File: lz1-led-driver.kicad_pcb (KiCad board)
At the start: 2 copper layers, 80 x 20.5 mm, 41 parts, among them J1 BarrelJack_3167288, J2 USB4105-GF-A, U1 MP2483DQ-LF-P, U2 AP62301Z6-7, U3 SM02B-SRSS-TB-LF-SN, U4 SM02B-SRSS-TB-LF-SN

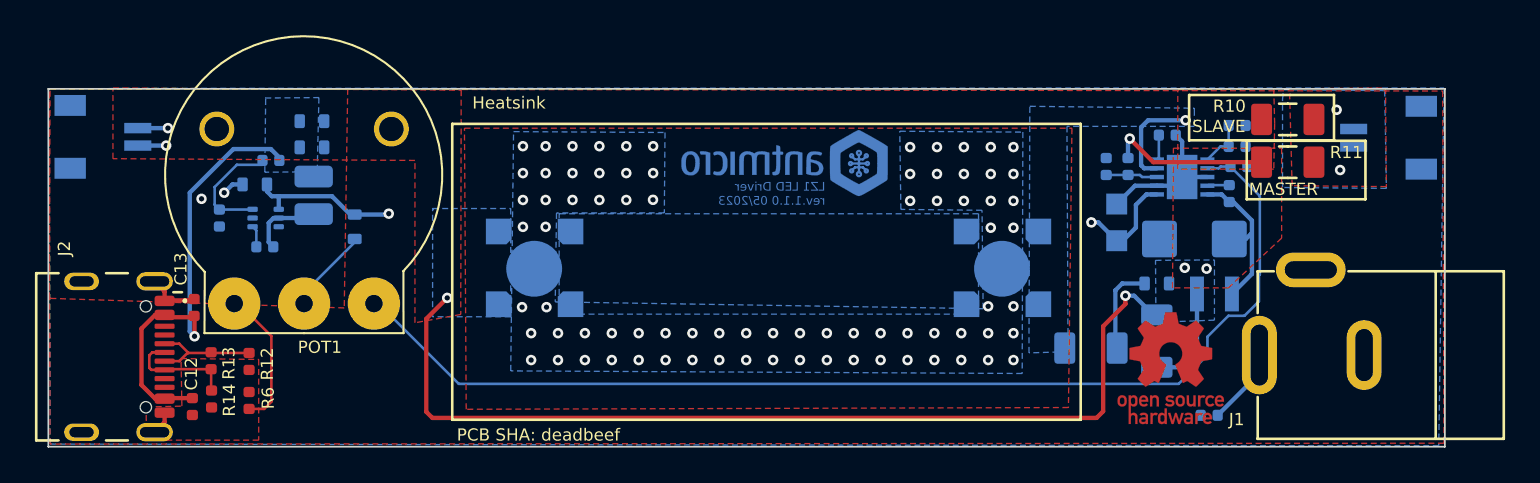
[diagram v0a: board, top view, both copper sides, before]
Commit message: Correct symbols and footprints with missing 3D models
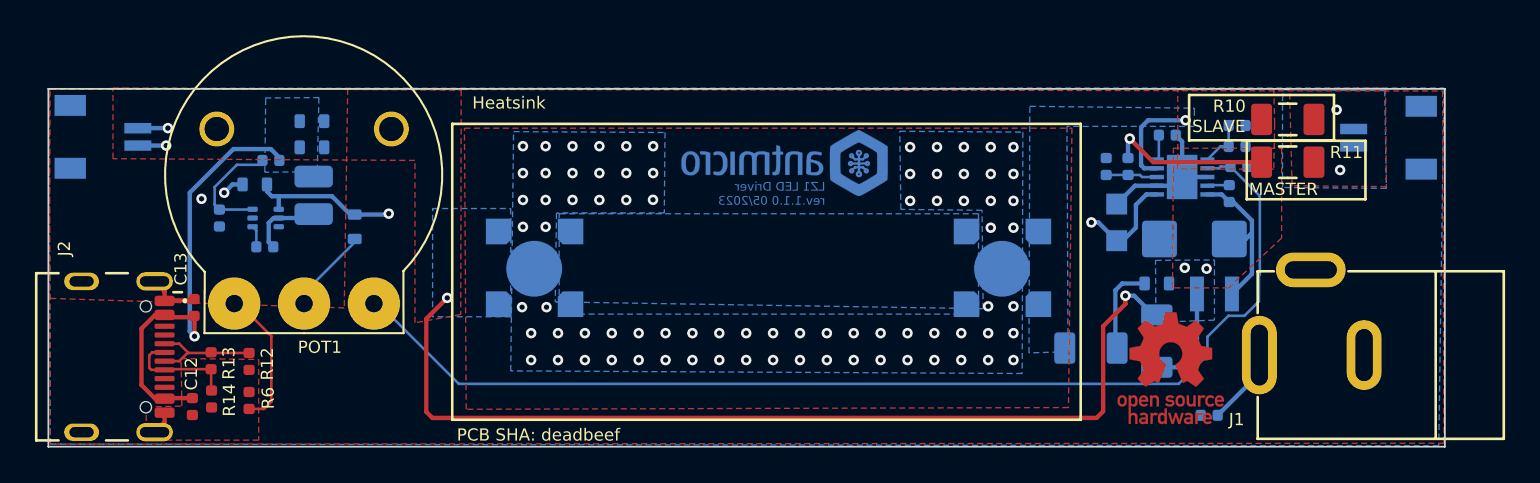
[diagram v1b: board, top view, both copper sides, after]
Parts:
- U3, U4: footprint antmicro-footprints:JST_SM02B-SRSS-TB(LF)(SN) -> antmicro-footprints:JST_SM02B-SRSS-TB-LF-SN

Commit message: Refresh standardization on schematic and PCB
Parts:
- added TP1: TP_1mm_SMD, antmicro-footprints:Testpoint_smd_1mm, B.Cu at (95.7, 49.2)
- C2: footprint antmicro-footprints:0603-cap -> antmicro-footprints:C_0603_1608Metric
- C4, C5: footprint antmicro-footprints:0402-cap -> antmicro-footprints:C_0402_1005Metric
- D2, D3: footprint antmicro-footprints:LZ1-00R802_4EP_4.4x4.4 -> antmicro-footprints:LED_IR_LZ1-00R802
- J2: value USB4105-GF-A -> USB-C_USB4105-GF-A
- POT1: value R0141-2-20k -> POT_20k_R0141-2-20k; footprint antmicro-footprints:Potentiometer_SRPassives_R0141-2_Horizontal -> antmicro-footprints:POT_R0141-2
- R1: footprint antmicro-footprints:1206-res -> antmicro-footprints:R_1206_3216Metric
- R2, R3, R8: footprint antmicro-footprints:0402-res -> antmicro-footprints:R_0402_1005Metric
- R5: footprint antmicro-footprints:0603-res -> antmicro-footprints:R_0603_1608Metric
- U1: footprint antmicro-footprints:MP2483DQ-LF-P -> antmicro-footprints:QFN-10-1EP_3x3mm_P0.5mm
- moved POT1 8.50 mm to (95.7, 52.8)
- moved L2 0.08 mm to (100.3, 46.6)
- renumbered U3 to J3, U4 to J4
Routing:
- net GND: track 18.1 -> 22.5 mm, vias 2 -> 5
- net Net-(TP1-Pad1): track 0.00 -> 2.10 mm

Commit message: Updated Value fields in selected footprints
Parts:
- POT1: value POT_20k_R0141-2-20k -> POT_R0141-2
- U1: value MP2483DQ-LF-P -> QFN-10-1EP_3x3mm_P0.5mm

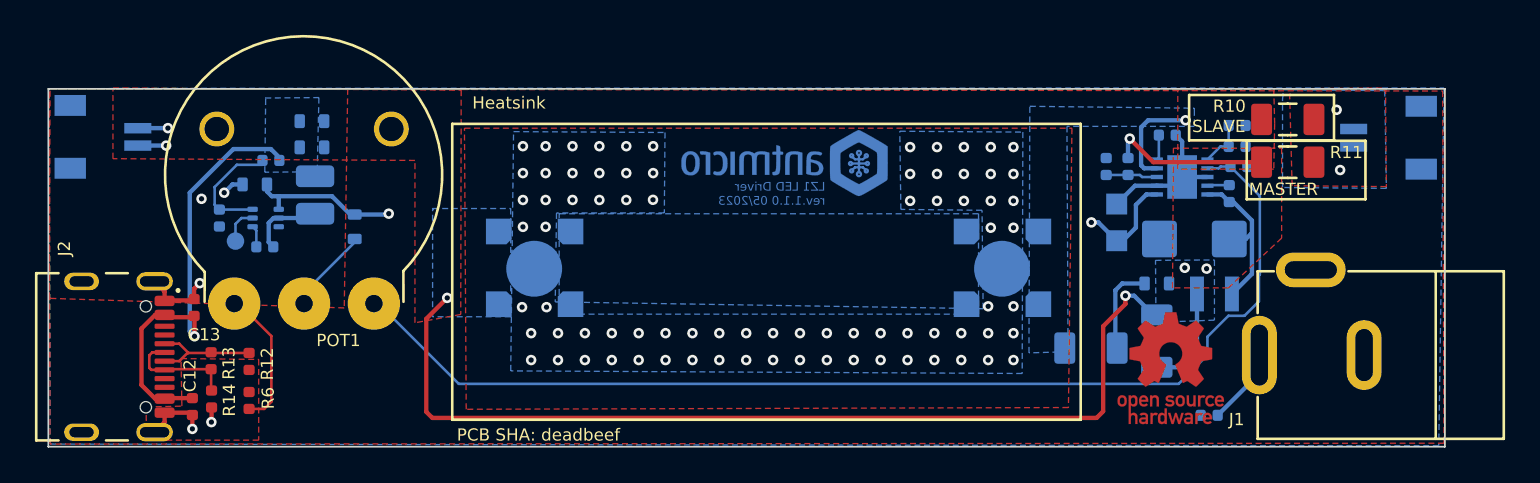
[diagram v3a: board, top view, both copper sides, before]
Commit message: Introduced schematic standardization
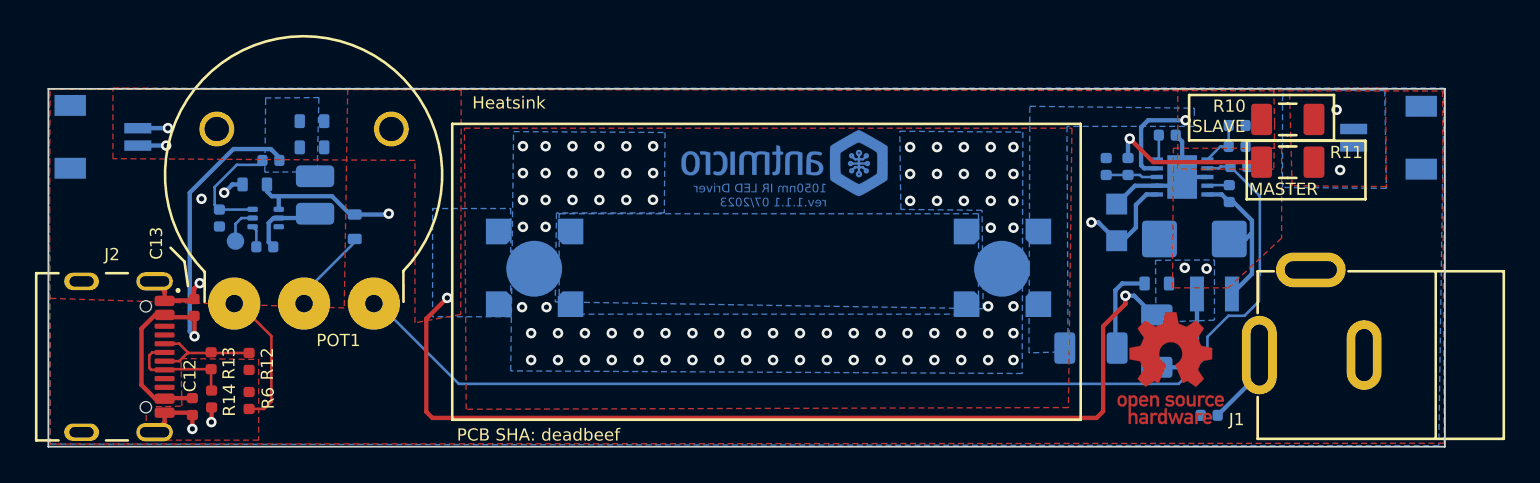
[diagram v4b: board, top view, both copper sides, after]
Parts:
- C1: footprint antmicro-footprints:0805-cap -> antmicro-footprints:C_0805_2012Metric
- J2: footprint antmicro-footprints:GCT_USB4105-GF-A -> antmicro-footprints:USB-C_GCT_USB4105-GF-A
- L1: value SRP2512A-4R7M -> L_4u7_1.5A_1008
- POT1: value POT_R0141-2 -> POT_20k_R0141-2-20k
- U1: value QFN-10-1EP_3x3mm_P0.5mm -> MP2483DQ-LF-P
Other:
- board text added: "1050nm IR LED Driver rev.${REVISION} 07/2023"
- board text removed: "LZ1 LED Driver rev.1.1.0 05/2023"

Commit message: [50954] Added CC resistors and OHP assets, updated README
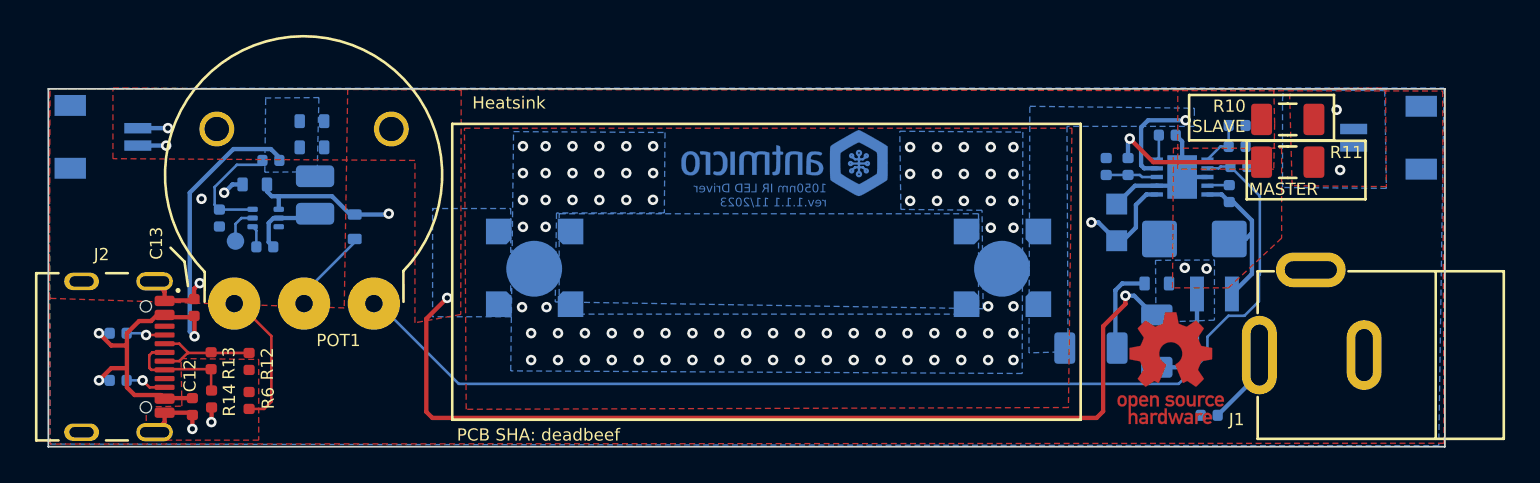
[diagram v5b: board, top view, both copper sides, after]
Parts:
- added R15: R_22k_0402, antmicro-footprints:R_0402_1005Metric, B.Cu at (89.0, 57.2)
- added R16: R_22k_0402, antmicro-footprints:R_0402_1005Metric, B.Cu at (89.0, 54.5)
- J2: value USB-C_USB4105-GF-A -> USB-C_GCT_USB4105-GF-A; footprint antmicro-footprints:USB-C_GCT_USB4105-GF-A -> antmicro-footprints:USB-C_Receptacle_GCT_USB4105-GF-A
- J3, J4: value SM02B-SRSS-TB-LF-SN -> JST_SH_1x2_SM02B-SRSS-TB-LF-SN; footprint antmicro-footprints:JST_SM02B-SRSS-TB-LF-SN -> antmicro-footprints:Conn_JST_SH_1x2_SM02B-SRSS-TB-LF-SN
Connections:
- J2 pad A5: unconnected-(J2-PadA5) -> Net-(R16-Pad1)
- J2 pad B5: unconnected-(J2-PadB5) -> Net-(R15-Pad1)
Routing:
- net /LED DRIVER & USB-C Power output/VBUS: track 25.4 -> 32.0 mm, vias 1 -> 3
- net Net-(R15-Pad1): track 0.00 -> 2.34 mm, vias 0 -> 1
- net Net-(R16-Pad1): track 0.00 -> 2.22 mm, vias 0 -> 1
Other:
- board text added: "1050nm IR LED Driver rev.${REVISION} 11/2023"
